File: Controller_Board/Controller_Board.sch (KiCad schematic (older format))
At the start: 45 parts, among them P1 USB_MICRO, U1 MCP73831, U2 LTC2941, U3 TCR2EF33, U4 ATMEGA32U4RC-A, U5 nRF24L01+, U6 I2C_DISPLAY, Y1 ABLS-8.000MHZ-B4-T

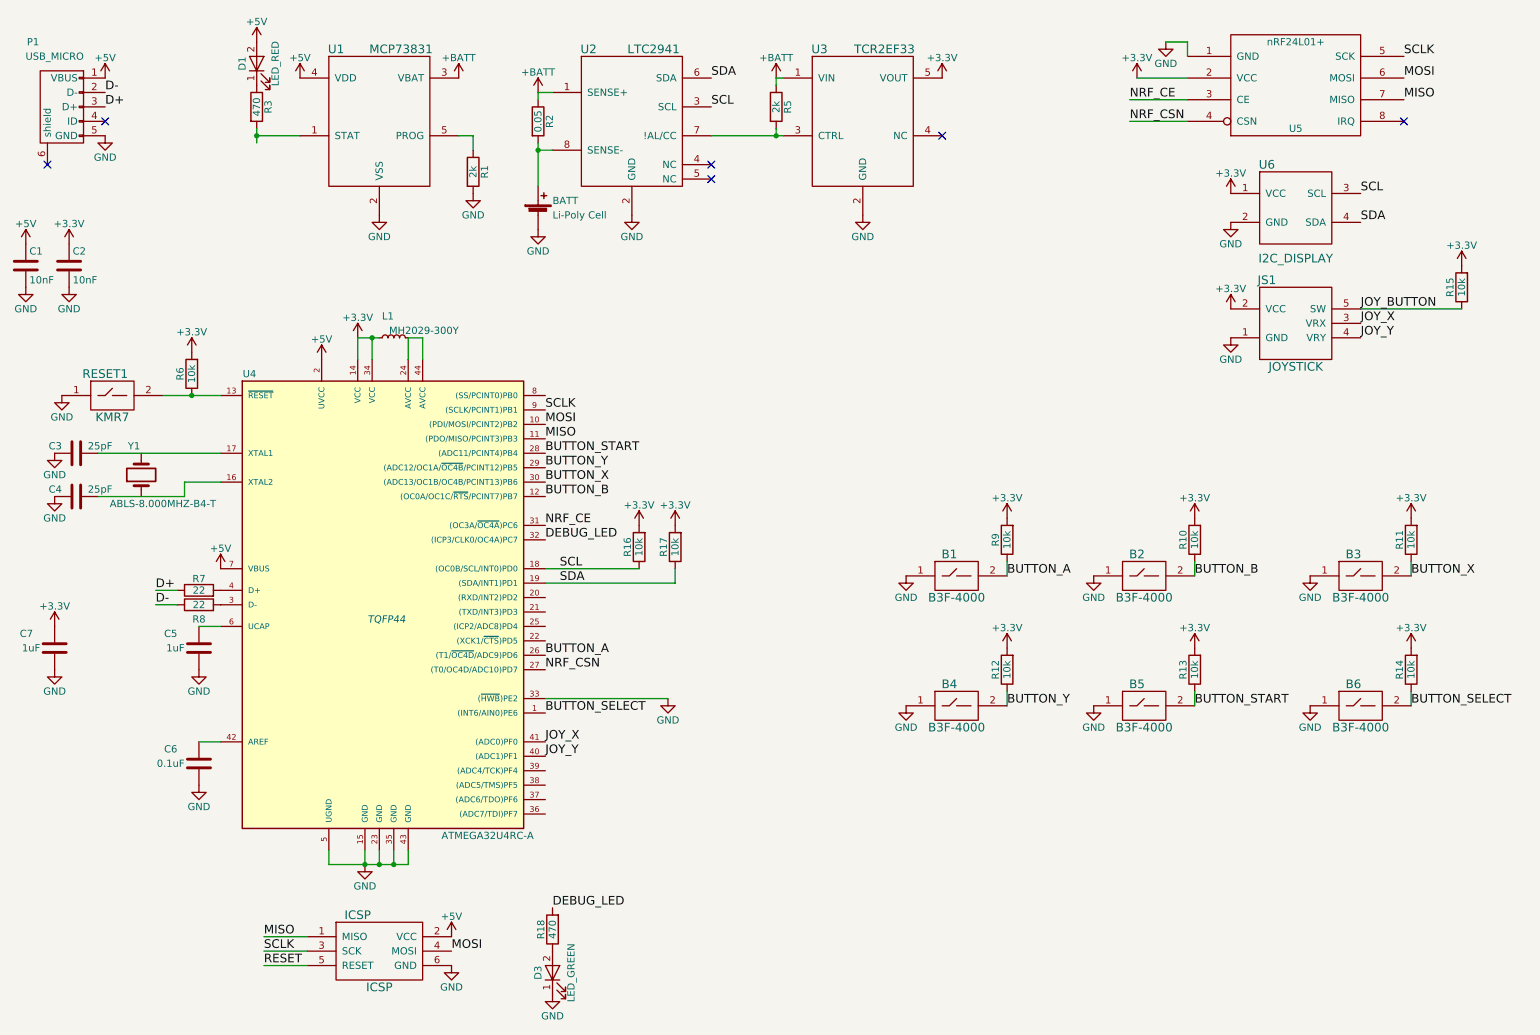
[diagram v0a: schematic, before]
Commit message: Placed almost all connections, power connections to follow
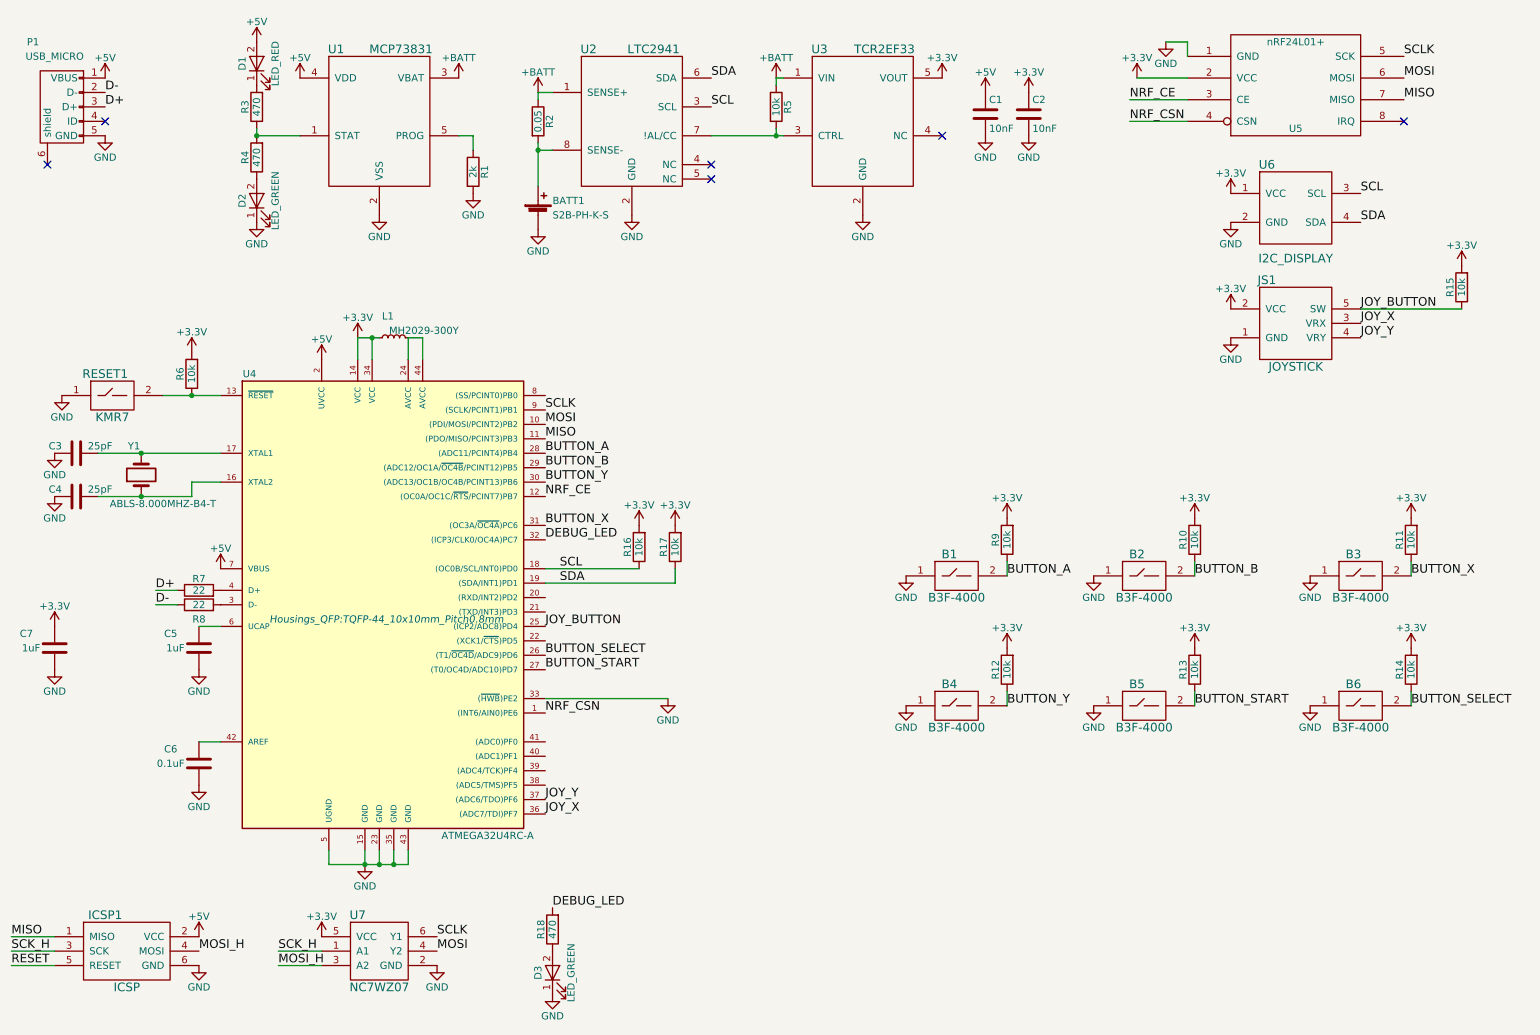
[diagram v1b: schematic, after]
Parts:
- added D2: LED_GREEN, Diodes_SMD:D_0603, symbol LED
- added R4: 470, Resistors_SMD:R_0603_HandSoldering, symbol R
- added U7: NC7WZ07, TO_SOT_Packages_SMD:SOT-363_SC-70-6, symbol NC7WZ07
- B1, B2, B3, B4, B5, B6: footprint (none) -> Buttons_Switches_ThroughHole:SW_PUSH-12mm
- BATT1: renamed from BATT; value Li-Poly Cell -> S2B-PH-K-S; footprint (none) -> Connectors_JST:JST_PH_S2B-PH-K_02x2.00mm_Angled
- C1, C2, C3, C4, C5, C6, C7: footprint (none) -> Capacitors_SMD:C_0603_HandSoldering
- D1, D3: footprint (none) -> Diodes_SMD:D_0603
- ICSP1: renamed from ICSP; footprint (none) -> Socket_Strips:Socket_Strip_Straight_2x03_Pitch2.54mm
- JS1: footprint (none) -> Socket_Strips:Socket_Strip_Straight_1x05_Pitch2.54mm
- L1: footprint (none) -> Resistors_SMD:R_0805_HandSoldering
- P1: footprint (none) -> Connect:USB_Micro-B
- R1, R10, R11, R12, R13, R14, R15, R16, R17, R18, R2, R3, R6, R7, R8, R9: footprint (none) -> Resistors_SMD:R_0603_HandSoldering
- R5: value 2k -> 10k; footprint (none) -> Resistors_SMD:R_0603_HandSoldering
- RESET1: footprint (none) -> Buttons_Switches_SMD:SW_SPST_KMR2
- U1: footprint (none) -> TO_SOT_Packages_SMD:SOT-23-5_HandSoldering
- U2: footprint (none) -> Housings_SSOP:MSOP-8_3x3mm_Pitch0.65mm
- U3: footprint (none) -> TO_SOT_Packages_SMD:TSOT-23-5_HandSoldering
- U4: footprint TQFP44 -> Housings_QFP:TQFP-44_10x10mm_Pitch0.8mm
- U5: footprint MODULE -> RF_Modules:nRF24L01_Breakout
- U6: footprint (none) -> Socket_Strips:Socket_Strip_Straight_1x04_Pitch2.54mm
- Y1: footprint (none) -> Crystals:Crystal_SMD_HC49-SD
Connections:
- net +3V3: now also U7.5 (VCC)
- net BUTTON_A: now also U4.28 ((ADC11/PCINT4)PB4); no longer U4.26 ((T1/~OC4D~/ADC9)PD6)
- net BUTTON_B: now also U4.29 ((ADC12/OC1A/~OC4B~/PCINT12)PB5); no longer U4.12 ((OC0A/OC1C/~RTS~/PCINT7)PB7)
- net BUTTON_SELECT: now also U4.26 ((T1/~OC4D~/ADC9)PD6); no longer U4.1 ((INT6/AIN0)PE6)
- net BUTTON_START: now also U4.27 ((T0/OC4D/ADC10)PD7); no longer U4.28 ((ADC11/PCINT4)PB4)
- net BUTTON_X: now also U4.31 ((OC3A/~OC4A~)PC6); no longer U4.30 ((ADC13/OC1B/OC4B/PCINT13)PB6)
- net BUTTON_Y: now also U4.30 ((ADC13/OC1B/OC4B/PCINT13)PB6); no longer U4.29 ((ADC12/OC1A/~OC4B~/PCINT12)PB5)
- net GND: now also D2.1 (K), U7.2 (GND)
- net JOY_BUTTON: now also U4.25 ((ICP2/ADC8)PD4)
- net JOY_X: now also U4.36 ((ADC7/TDI)PF7); no longer U4.41 ((ADC0)PF0)
- net JOY_Y: now also U4.37 ((ADC6/TDO)PF6); no longer U4.40 ((ADC1)PF1)
- net MOSI: now also U7.4 (Y2); no longer ICSP1.4 (MOSI)
- net NRF_CE: now also U4.12 ((OC0A/OC1C/~RTS~/PCINT7)PB7); no longer U4.31 ((OC3A/~OC4A~)PC6)
- net NRF_CSN: now also U4.1 ((INT6/AIN0)PE6); no longer U4.27 ((T0/OC4D/ADC10)PD7)
- net SCLK: now also U7.6 (Y1); no longer ICSP1.3 (SCK)
- net at U1.1 (STAT): now also R3.1, R4.2; no longer R3.2
- net at D1.1 (K): now also R3.2; no longer R3.1
- net at C4.2, U4.16 (XTAL2): now also Y1.1
- net at C3.2, U4.17 (XTAL1): now also Y1.2
- new net: D2.2 (A), R4.1
- new net MOSI_H: ICSP1.4 (MOSI), U7.3 (A2)
- new net SCK_H: ICSP1.3 (SCK), U7.1 (A1)
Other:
- moved on the sheet: C1, C2, ICSP1

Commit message: Updated Controller Board with shoulder buttons, mounting holes, slightly altered pinout, second analog stick option, dual button footprints.... I really should have done this in stages...
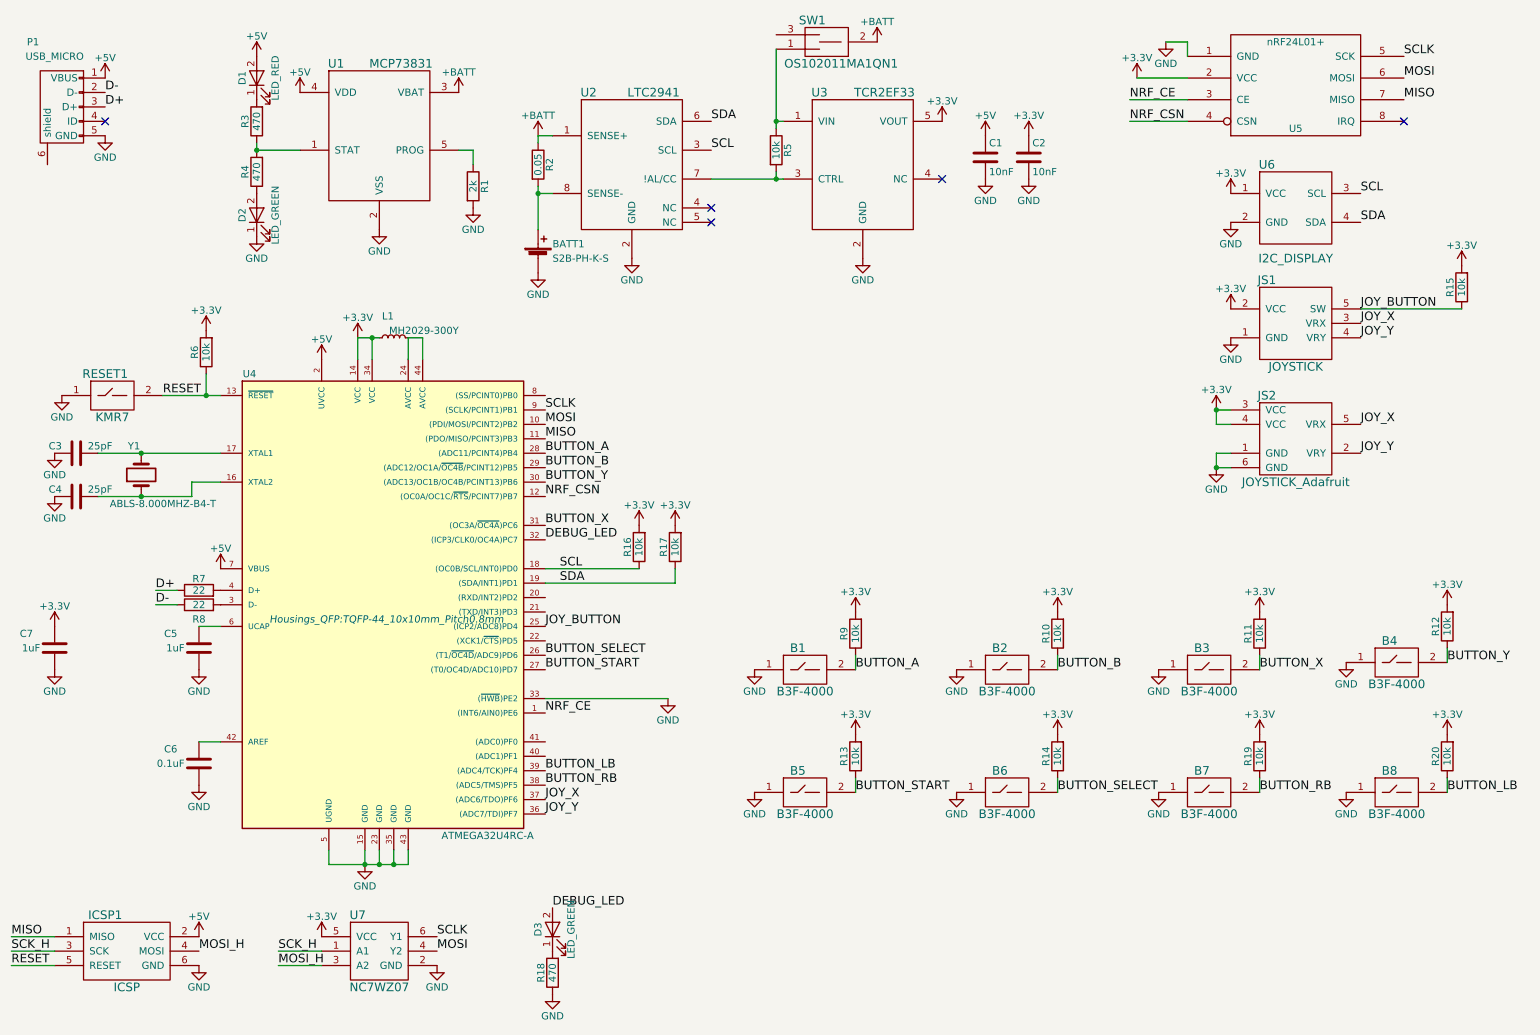
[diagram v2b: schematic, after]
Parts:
- added B7, B8: B3F-4000, YouControl:Button_Right_Angle, symbol B3F-4000
- added JS2: JOYSTICK_Adafruit, YouControl:Joystick_Adafruit, symbol JOYSTICK_Adafruit
- added R19, R20: 10k, Resistors_SMD:R_0603_HandSoldering, symbol R
- added SW1: OS102011MA1QN1, YouControl:MHSS1105, symbol OS102011MA1QN1
- B1, B2, B3, B4, B5, B6: footprint Buttons_Switches_ThroughHole:SW_PUSH-12mm -> YouControl:Button_Dual
- JS1: footprint Socket_Strips:Socket_Strip_Straight_1x05_Pitch2.54mm -> YouControl:Joystick_PlayStation
- U6: footprint Socket_Strips:Socket_Strip_Straight_1x04_Pitch2.54mm -> YouControl:I2C_Screen
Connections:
- net +3V3: now also JS2.3 (VCC), JS2.4 (VCC), R19.2, R20.2
- net +BATT: now also SW1.2; no longer R5.1, U3.1 (VIN)
- net DEBUG_LED: now also D3.2 (A); no longer R18.2
- net GND: now also R18.1, B7.1, B8.1, JS2.1 (GND), JS2.6 (GND); no longer D3.1 (K)
- net JOY_X: now also U4.37 ((ADC6/TDO)PF6), JS2.5 (VRX); no longer U4.36 ((ADC7/TDI)PF7)
- net JOY_Y: now also U4.36 ((ADC7/TDI)PF7), JS2.2 (VRY); no longer U4.37 ((ADC6/TDO)PF6)
- net NRF_CE: now also U4.1 ((INT6/AIN0)PE6); no longer U4.12 ((OC0A/OC1C/~RTS~/PCINT7)PB7)
- net NRF_CSN: now also U4.12 ((OC0A/OC1C/~RTS~/PCINT7)PB7); no longer U4.1 ((INT6/AIN0)PE6)
- net RESET: now also R6.1, RESET1.2, U4.13 (~RESET~)
- net BUTTON_RB: now reaches U4.38 ((ADC5/TMS)PF5)
- net BUTTON_RB: now also B7.2, R19.1
- net BUTTON_LB: now reaches U4.39 ((ADC4/TCK)PF4)
- net BUTTON_LB: now also B8.2, R20.1
- new net: R5.1, SW1.1, U3.1 (VIN)
- new net: D3.1 (K), R18.2
- no-connect marks 6 -> 5
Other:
- moved on the sheet: B1, B2, B3, B4, B5, B6, BATT1, C1, C2, D1, D2, D3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
